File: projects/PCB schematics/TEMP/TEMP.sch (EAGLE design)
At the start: 0 parts

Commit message: POWER - Initial drafts.
Adding in initial place holders for DCDC, 5V, and 12V. Completed most of TEMP.
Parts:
- added IC1, IC10, IC2, IC3, IC4, IC5, IC6, IC7, IC8, IC9: 4051D, 40xx:4051D
- added J1, J2: SAMTEC-TFM-120-02-X-D-LCJ, SAMTEC-TFM-120-02-X-D-LC:SAMTEC-TFM-120-02-X-D-LCJ
- added R1, R2, R3, R4: (no value), rcl:R-US_R0805
- added X2: 5566-4, con-molex:5566-4
- added X3: 5566-2, con-molex:5566-2
- added X4: 5566-10, con-molex:5566-10
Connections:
- new net CS_A: IC10A.A, IC1A.A, IC2A.A, IC3A.A, IC4A.A, IC5A.A, IC6A.A, IC7A.A, IC8A.A, IC9A.A, R2.2, X2-1.S
- new net CS_B: IC10A.B, IC1A.B, IC2A.B, IC3A.B, IC4A.B, IC5A.B, IC6A.B, IC7A.B, IC8A.B, IC9A.B, R3.2, X2-2.S
- new net CS_C: IC10A.C, IC1A.C, IC2A.C, IC3A.C, IC4A.C, IC5A.C, IC6A.C, IC7A.C, IC8A.C, IC9A.C, R4.2, X2-3.S
- new net GND: R1.1, R2.1, R3.1, R4.1, X3-2.S
- new net INH: IC10A.INH, IC1A.INH, IC2A.INH, IC3A.INH, IC4A.INH, IC5A.INH, IC6A.INH, IC7A.INH, IC8A.INH, IC9A.INH, R1.2
- new net TEMP1: IC1A.X0, J1.1
- new net TEMP10: IC2A.X1, J1.10
- new net TEMP11: IC2A.X2, J1.11
- new net TEMP12: IC2A.X3, J1.12
- new net TEMP13: IC2A.X4, J1.13
- new net TEMP14: IC2A.X5, J1.14
- new net TEMP15: IC2A.X6, J1.15
- new net TEMP16: IC2A.X7, J1.16
- new net TEMP17: IC3A.X0, J1.17
- new net TEMP18: IC3A.X1, J1.18
- new net TEMP19: IC3A.X2, J1.19
- new net TEMP2: IC1A.X1, J1.2
- new net TEMP20: IC3A.X3, J1.20
- new net TEMP21: IC3A.X4, J1.21
- new net TEMP22: IC3A.X5, J1.22
- new net TEMP23: IC3A.X6, J1.23
- new net TEMP24: IC3A.X7, J1.24
- new net TEMP25: IC5A.X0, J1.25
- new net TEMP26: IC5A.X1, J1.26
- new net TEMP27: IC5A.X2, J1.27
- new net TEMP28: IC5A.X3, J1.28
- new net TEMP29: IC5A.X4, J1.29
- new net TEMP3: IC1A.X2, J1.3
- new net TEMP30: IC5A.X5, J1.30
- new net TEMP31: IC5A.X6, J1.31
- new net TEMP32: IC5A.X7, J1.32
- new net TEMP33: IC6A.X0, J1.33
- new net TEMP34: IC6A.X1, J1.34
- new net TEMP35: IC6A.X2, J1.35
- new net TEMP36: IC6A.X3, J1.36
- new net TEMP37: IC6A.X4, J1.37
- new net TEMP38: IC6A.X5, J1.38
- new net TEMP39: IC6A.X6, J1.39
- new net TEMP4: IC1A.X3, J1.4
- new net TEMP40: IC6A.X7, J1.40
- new net TEMP41: IC7A.X0, J2.1
- new net TEMP42: IC7A.X1, J2.2
- new net TEMP43: IC7A.X2, J2.3
- new net TEMP44: IC7A.X3, J2.4
- new net TEMP45: IC7A.X4, J2.5
- new net TEMP46: IC7A.X5, J2.6
- new net TEMP47: IC7A.X6, J2.7
- new net TEMP48: IC7A.X7, J2.8
- new net TEMP49: IC4A.X0, J2.9
- new net TEMP5: IC1A.X4, J1.5
- new net TEMP50: IC4A.X1, J2.10
- new net TEMP51: IC4A.X2, J2.11
- new net TEMP52: IC4A.X3, J2.12
- new net TEMP53: IC4A.X4, J2.13
- new net TEMP54: IC4A.X5, J2.14
- new net TEMP55: IC4A.X6, J2.15
- new net TEMP56: IC4A.X7, J2.16
- new net TEMP57: IC9A.X0, J2.17
- new net TEMP58: IC9A.X1, J2.18
- new net TEMP59: IC9A.X2, J2.19
- new net TEMP6: IC1A.X5, J1.6
- new net TEMP60: IC9A.X3, J2.20
- new net TEMP61: IC9A.X4, J2.21
- new net TEMP62: IC9A.X5, J2.22
- new net TEMP63: IC9A.X6, J2.23
- new net TEMP64: IC9A.X7, J2.24
- new net TEMP65: IC8A.X0, J2.25
- new net TEMP66: IC8A.X1, J2.26
- new net TEMP67: IC8A.X2, J2.27
- new net TEMP68: IC8A.X3, J2.28
- new net TEMP69: IC8A.X4, J2.29
- new net TEMP7: IC1A.X6, J1.7
- new net TEMP70: IC8A.X5, J2.30
- new net TEMP71: IC8A.X6, J2.31
- new net TEMP72: IC8A.X7, J2.32
- new net TEMP73: IC10A.X0, J2.33
- new net TEMP74: IC10A.X1, J2.34
- new net TEMP75: IC10A.X2, J2.35
- new net TEMP76: IC10A.X3, J2.36
- new net TEMP77: IC10A.X4, J2.37
- new net TEMP78: IC10A.X5, J2.38
- new net TEMP79: IC10A.X6, J2.39
- new net TEMP8: IC1A.X7, J1.8
- new net TEMP80: IC10A.X7, J2.40
- new net TEMP9: IC2A.X0, J1.9
- new net TEMP_OUT1: IC1A.X, X4-1.S
- new net TEMP_OUT10: IC10A.X, X4-10.S
- new net TEMP_OUT2: IC2A.X, X4-2.S
- new net TEMP_OUT3: IC3A.X, X4-3.S
- new net TEMP_OUT4: IC5A.X, X4-4.S
- new net TEMP_OUT5: IC6A.X, X4-5.S
- new net TEMP_OUT6: IC7A.X, X4-6.S
- new net TEMP_OUT7: IC4A.X, X4-7.S
- new net TEMP_OUT8: IC9A.X, X4-8.S
- new net TEMP_OUT9: IC8A.X, X4-9.S
- new net VCC: X3-1.S

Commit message: TEMP - Initial board placement.
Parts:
- removed IC1, IC10, IC2, IC3, IC4, IC5, IC6, IC7, IC8, IC9: 4051D, 40xx:4051D
- removed J2: SAMTEC-TFM-120-02-X-D-LCJ, SAMTEC-TFM-120-02-X-D-LC:SAMTEC-TFM-120-02-X-D-LCJ
- added MUX1, MUX2, MUX3, MUX4, MUX5: 4051D, 40xx:4051D
- added SH1, SH2, SH3: SHORTT5, shorts:SHORTT5
- added X1: 5566-4, con-molex:5566-4
- R1, R2, R3, R4: value (none) -> 50k
- X4: value 5566-10 -> 5566-6; device con-molex:5566-10 -> con-molex:5566-6
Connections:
- removed net CS_A: IC10A.A, IC1A.A, IC2A.A, IC3A.A, IC4A.A, IC5A.A, IC6A.A, IC7A.A, IC8A.A, IC9A.A, R2.2, X2-1.S
- removed net CS_B: IC10A.B, IC1A.B, IC2A.B, IC3A.B, IC4A.B, IC5A.B, IC6A.B, IC7A.B, IC8A.B, IC9A.B, R3.2, X2-2.S
- removed net CS_C: IC10A.C, IC1A.C, IC2A.C, IC3A.C, IC4A.C, IC5A.C, IC6A.C, IC7A.C, IC8A.C, IC9A.C, R4.2, X2-3.S
- removed net TEMP41: IC7A.X0, J2.1
- removed net TEMP42: IC7A.X1, J2.2
- removed net TEMP43: IC7A.X2, J2.3
- removed net TEMP44: IC7A.X3, J2.4
- removed net TEMP45: IC7A.X4, J2.5
- removed net TEMP46: IC7A.X5, J2.6
- removed net TEMP47: IC7A.X6, J2.7
- removed net TEMP48: IC7A.X7, J2.8
- removed net TEMP49: IC4A.X0, J2.9
- removed net TEMP50: IC4A.X1, J2.10
- removed net TEMP51: IC4A.X2, J2.11
- removed net TEMP52: IC4A.X3, J2.12
- removed net TEMP53: IC4A.X4, J2.13
- removed net TEMP54: IC4A.X5, J2.14
- removed net TEMP55: IC4A.X6, J2.15
- removed net TEMP56: IC4A.X7, J2.16
- removed net TEMP57: IC9A.X0, J2.17
- removed net TEMP58: IC9A.X1, J2.18
- removed net TEMP59: IC9A.X2, J2.19
- removed net TEMP60: IC9A.X3, J2.20
- removed net TEMP61: IC9A.X4, J2.21
- removed net TEMP62: IC9A.X5, J2.22
- removed net TEMP63: IC9A.X6, J2.23
- removed net TEMP64: IC9A.X7, J2.24
- removed net TEMP65: IC8A.X0, J2.25
- removed net TEMP66: IC8A.X1, J2.26
- removed net TEMP67: IC8A.X2, J2.27
- removed net TEMP68: IC8A.X3, J2.28
- removed net TEMP69: IC8A.X4, J2.29
- removed net TEMP70: IC8A.X5, J2.30
- removed net TEMP71: IC8A.X6, J2.31
- removed net TEMP72: IC8A.X7, J2.32
- removed net TEMP73: IC10A.X0, J2.33
- removed net TEMP74: IC10A.X1, J2.34
- removed net TEMP75: IC10A.X2, J2.35
- removed net TEMP76: IC10A.X3, J2.36
- removed net TEMP77: IC10A.X4, J2.37
- removed net TEMP78: IC10A.X5, J2.38
- removed net TEMP79: IC10A.X6, J2.39
- removed net TEMP80: IC10A.X7, J2.40
- removed net TEMP_OUT10: IC10A.X, X4-10.S
- removed net TEMP_OUT6: IC7A.X, X4-6.S
- removed net TEMP_OUT7: IC4A.X, X4-7.S
- removed net TEMP_OUT8: IC9A.X, X4-8.S
- removed net TEMP_OUT9: IC8A.X, X4-9.S
- new net CS_A_IN: MUX1A.A, MUX2A.A, MUX3A.A, MUX4A.A, MUX5A.A, R2.2, SH1.P$1, X2-1.S
- new net CS_A_OUT: SH1.P$2, X1-1.S
- new net CS_B_IN: MUX1A.B, MUX2A.B, MUX3A.B, MUX4A.B, MUX5A.B, R3.2, SH2.P$1, X2-2.S
- new net CS_B_OUT: SH2.P$2, X1-2.S
- new net CS_C_IN: MUX1A.C, MUX2A.C, MUX3A.C, MUX4A.C, MUX5A.C, R4.2, SH3.P$1, X2-3.S
- new net CS_C_OUT: SH3.P$2, X1-3.S
- net GND: now also MUX1P.GND, MUX1P.VEE, MUX2P.GND, MUX2P.VEE, MUX3P.GND, MUX3P.VEE, MUX4P.GND, MUX4P.VEE, MUX5P.GND, MUX5P.VEE
- net INH: now also MUX1A.INH, MUX2A.INH, MUX3A.INH, MUX4A.INH, MUX5A.INH; no longer IC10A.INH, IC1A.INH, IC2A.INH, IC3A.INH, IC4A.INH, IC5A.INH, IC6A.INH, IC7A.INH, IC8A.INH, IC9A.INH
- net TEMP1: now also MUX1A.X0; no longer IC1A.X0
- net TEMP10: now also MUX2A.X1; no longer IC2A.X1
- net TEMP11: now also MUX2A.X2; no longer IC2A.X2
- net TEMP12: now also MUX2A.X3; no longer IC2A.X3
- net TEMP13: now also MUX2A.X4; no longer IC2A.X4
- net TEMP14: now also MUX2A.X5; no longer IC2A.X5
- net TEMP15: now also MUX2A.X6; no longer IC2A.X6
- net TEMP16: now also MUX2A.X7; no longer IC2A.X7
- net TEMP17: now also MUX3A.X0; no longer IC3A.X0
- net TEMP18: now also MUX3A.X1; no longer IC3A.X1
- net TEMP19: now also MUX3A.X2; no longer IC3A.X2
- net TEMP2: now also MUX1A.X1; no longer IC1A.X1
- net TEMP20: now also MUX3A.X3; no longer IC3A.X3
- net TEMP21: now also MUX3A.X4; no longer IC3A.X4
- net TEMP22: now also MUX3A.X5; no longer IC3A.X5
- net TEMP23: now also MUX3A.X6; no longer IC3A.X6
- net TEMP24: now also MUX3A.X7; no longer IC3A.X7
- net TEMP25: now also MUX4A.X0; no longer IC5A.X0
- net TEMP26: now also MUX4A.X1; no longer IC5A.X1
- net TEMP27: now also MUX4A.X2; no longer IC5A.X2
- net TEMP28: now also MUX4A.X3; no longer IC5A.X3
- net TEMP29: now also MUX4A.X4; no longer IC5A.X4
- net TEMP3: now also MUX1A.X2; no longer IC1A.X2
- net TEMP30: now also MUX4A.X5; no longer IC5A.X5
- net TEMP31: now also MUX4A.X6; no longer IC5A.X6
- net TEMP32: now also MUX4A.X7; no longer IC5A.X7
- net TEMP33: now also MUX5A.X0; no longer IC6A.X0
- net TEMP34: now also MUX5A.X1; no longer IC6A.X1
- net TEMP35: now also MUX5A.X2; no longer IC6A.X2
- net TEMP36: now also MUX5A.X3; no longer IC6A.X3
- net TEMP37: now also MUX5A.X4; no longer IC6A.X4
- net TEMP38: now also MUX5A.X5; no longer IC6A.X5
- net TEMP39: now also MUX5A.X6; no longer IC6A.X6
- net TEMP4: now also MUX1A.X3; no longer IC1A.X3
- net TEMP40: now also MUX5A.X7; no longer IC6A.X7
- net TEMP5: now also MUX1A.X4; no longer IC1A.X4
- net TEMP6: now also MUX1A.X5; no longer IC1A.X5
- net TEMP7: now also MUX1A.X6; no longer IC1A.X6
- net TEMP8: now also MUX1A.X7; no longer IC1A.X7
- net TEMP9: now also MUX2A.X0; no longer IC2A.X0
- net TEMP_OUT1: now also MUX1A.X; no longer IC1A.X
- net TEMP_OUT2: now also MUX2A.X; no longer IC2A.X
- net TEMP_OUT3: now also MUX3A.X; no longer IC3A.X
- net TEMP_OUT4: now also MUX4A.X; no longer IC5A.X
- net TEMP_OUT5: now also MUX5A.X; no longer IC6A.X
- net VCC: now also MUX1P.VCC, MUX2P.VCC
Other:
- moved on the sheet: J1, R1, R2, R3, R4, X2-1, X2-2, X2-3, X2-4, X3-1, X3-2, X4-1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

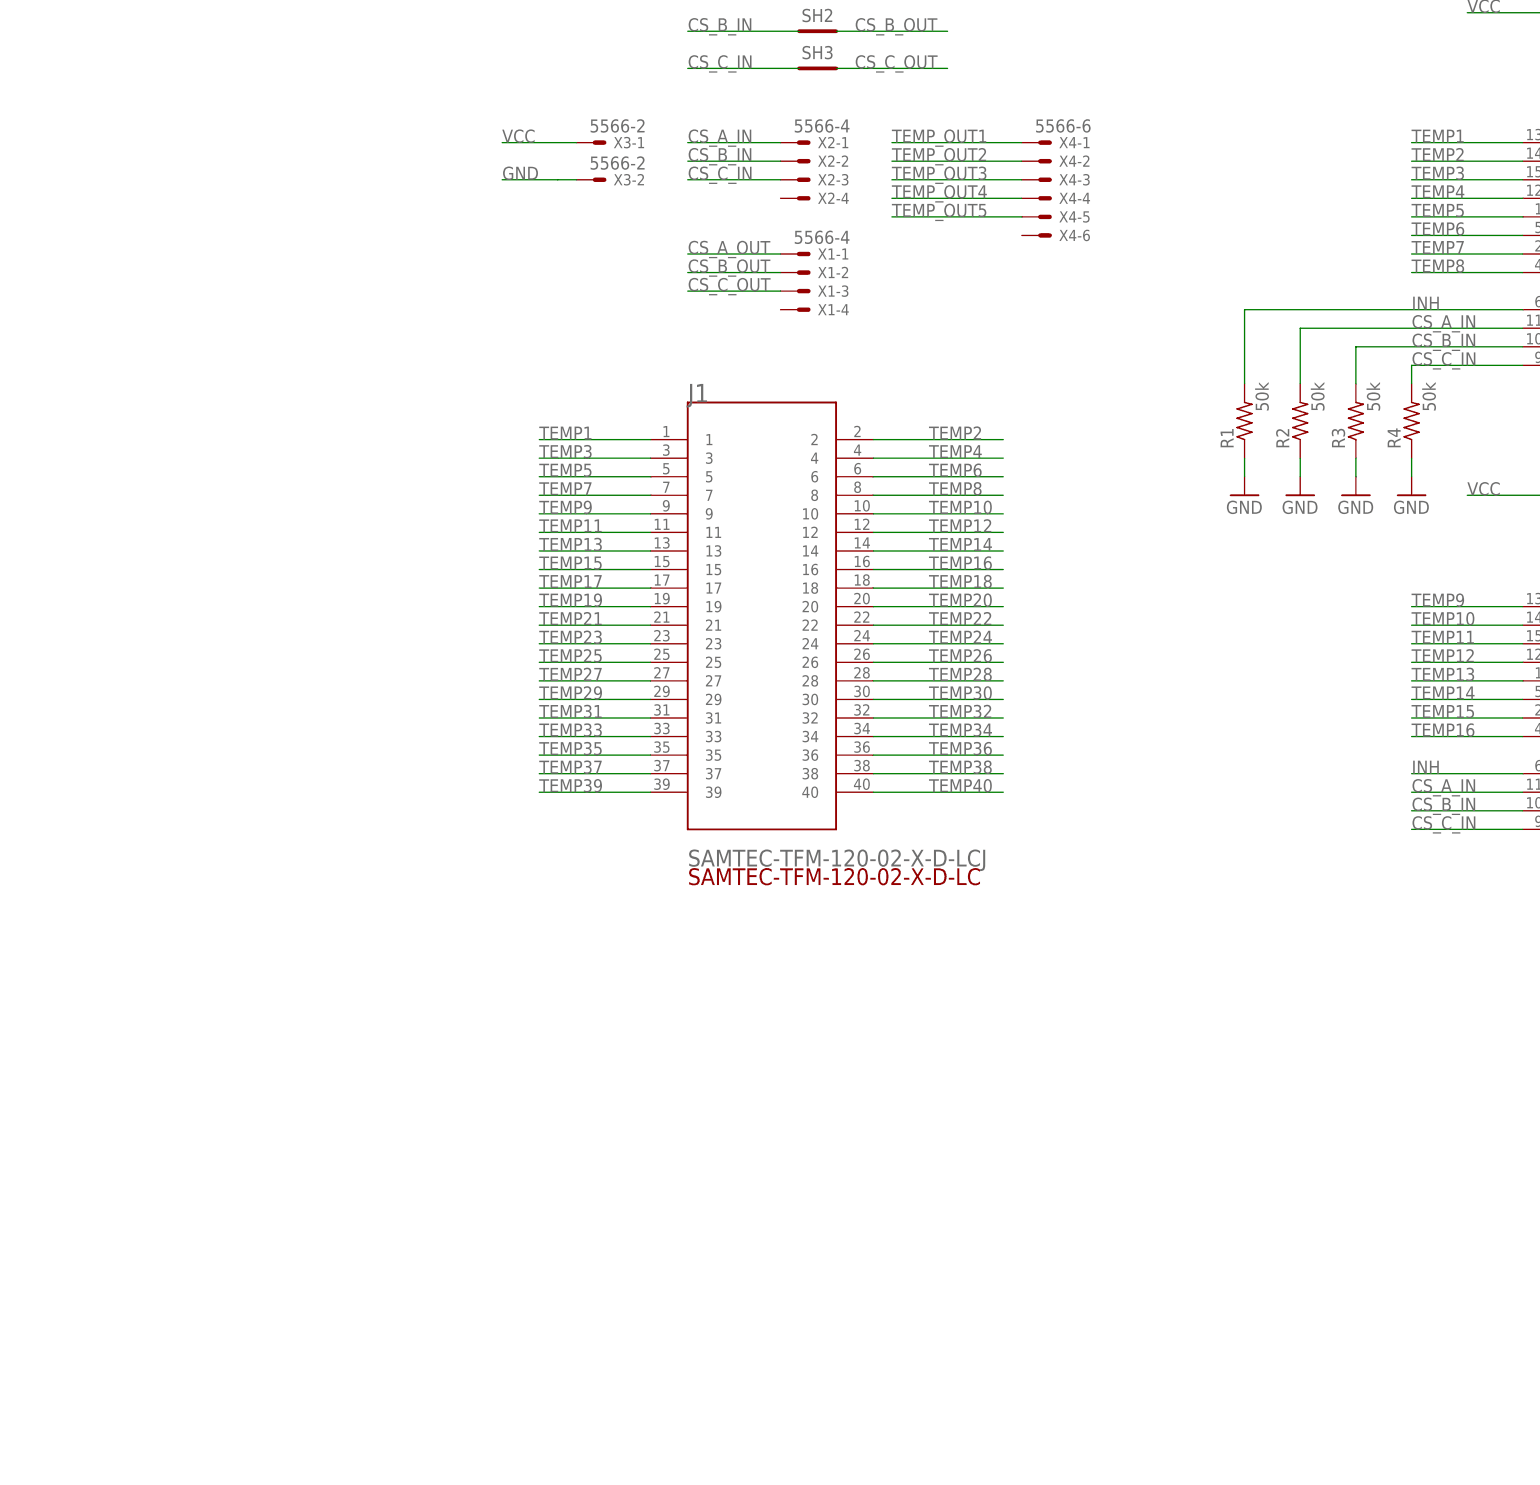
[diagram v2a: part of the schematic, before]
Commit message: TEMP - Energus components added in.
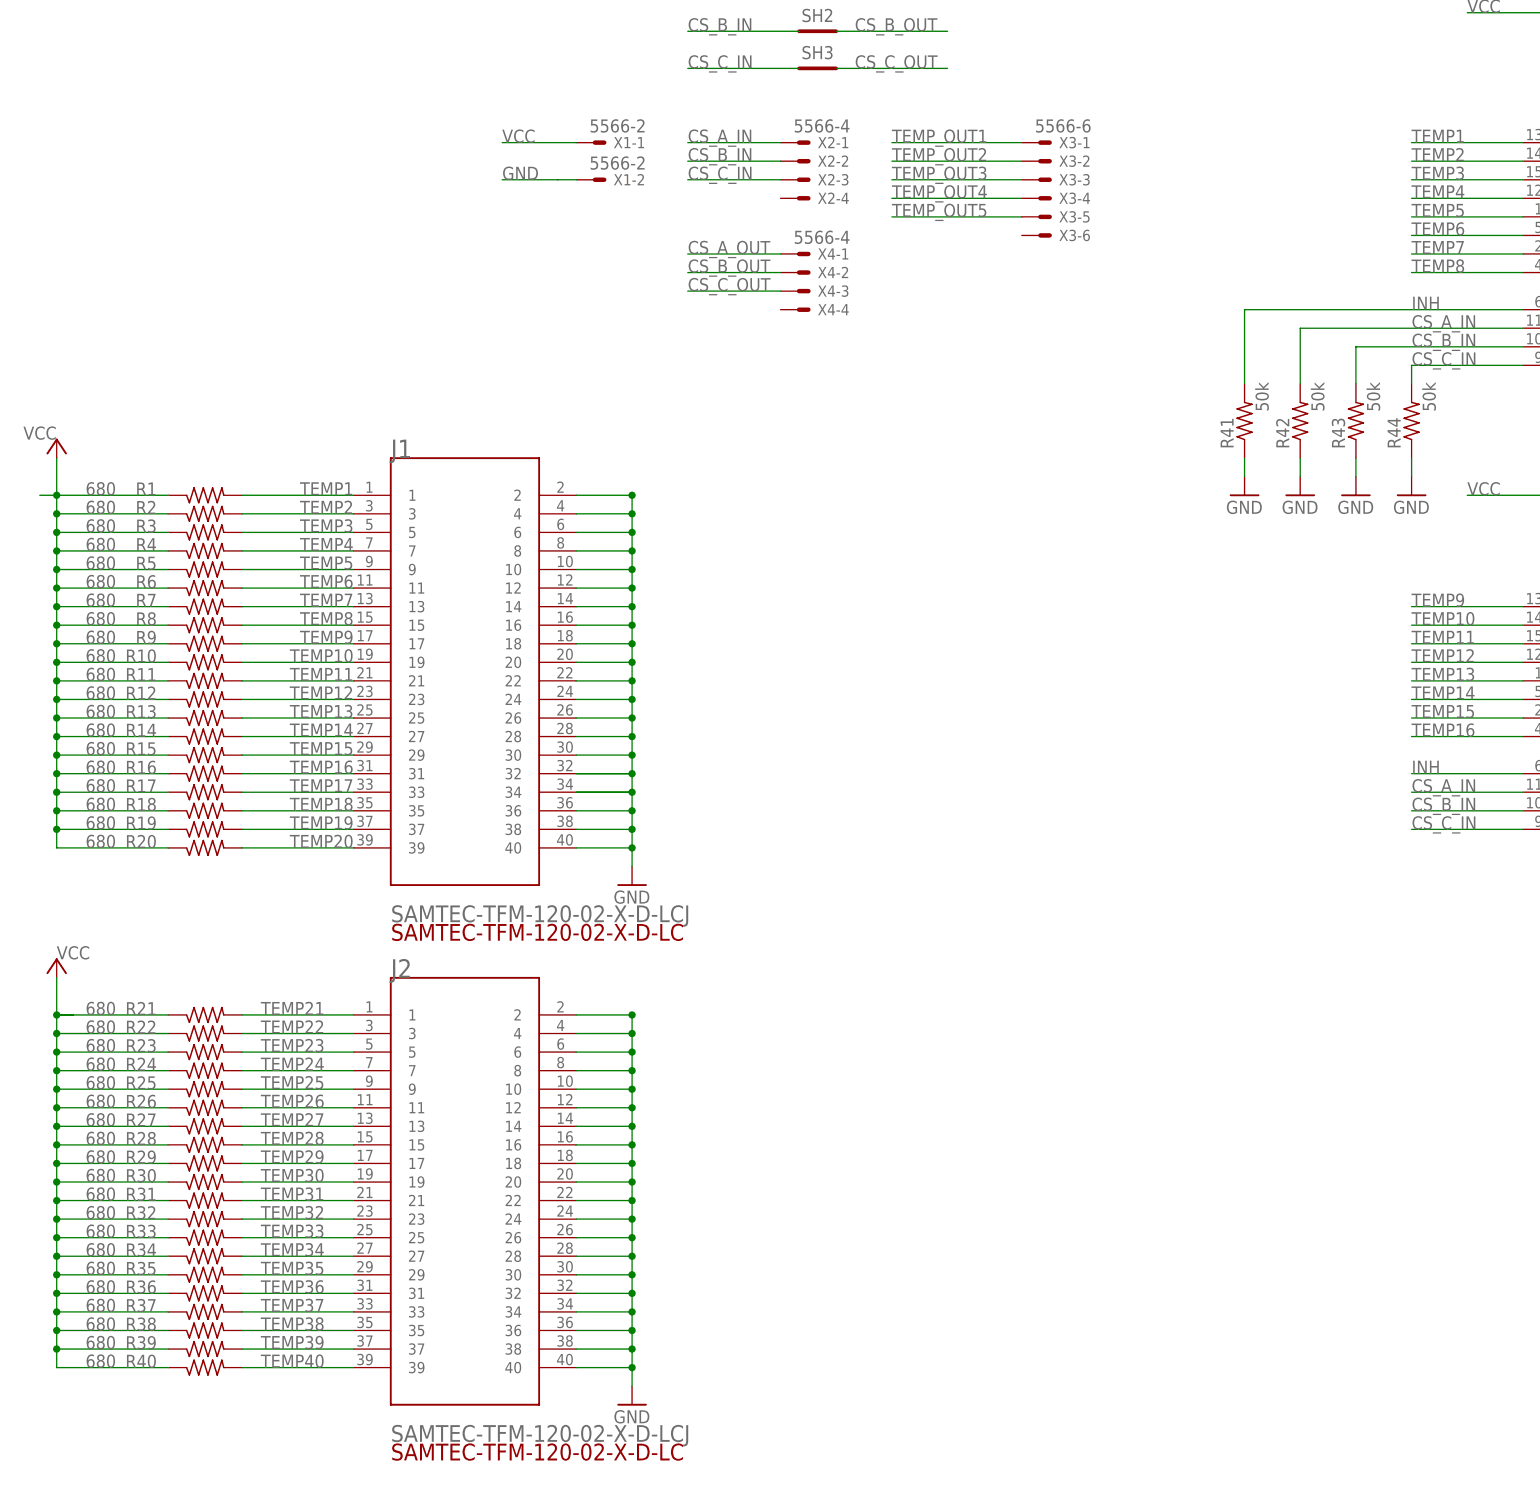
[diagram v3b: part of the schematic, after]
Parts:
- added J2: SAMTEC-TFM-120-02-X-D-LCJ, SAMTEC-TFM-120-02-X-D-LC:SAMTEC-TFM-120-02-X-D-LCJ
- added R10, R11, R12, R13, R14, R15, R16, R17, R18, R19, R20, R21, R22, R23, R24, R25, R26, R27, R28, R29, R30, R31, R32, R33, R34, R35, R36, R37, R38, R39, R40, R5, R6, R7, R8, R9: 680, rcl:R-US_R0805
- added R41, R42, R43, R44: 50k, rcl:R-US_R0805
- R1, R2, R3, R4: value 50k -> 680
- X1: value 5566-4 -> 5566-2; device con-molex:5566-4 -> con-molex:5566-2
- X3: value 5566-2 -> 5566-6; device con-molex:5566-2 -> con-molex:5566-6
- X4: value 5566-6 -> 5566-4; device con-molex:5566-6 -> con-molex:5566-4
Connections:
- net CS_A_IN: now also R42.2; no longer R2.2
- net CS_A_OUT: now also X4-1.S; no longer X1-1.S
- net CS_B_IN: now also R43.2; no longer R3.2
- net CS_B_OUT: now also X4-2.S; no longer X1-2.S
- net CS_C_IN: now also R44.2; no longer R4.2
- net CS_C_OUT: now also X4-3.S; no longer X1-3.S
- net GND: now also J1.10, J1.12, J1.14, J1.16, J1.18, J1.2, J1.20, J1.22, J1.24, J1.26, J1.28, J1.30, J1.32, J1.34, J1.36, J1.38, J1.4, J1.40, J1.6, J1.8, J2.10, J2.12, J2.14, J2.16, J2.18, J2.2, J2.20, J2.22, J2.24, J2.26, J2.28, J2.30, J2.32, J2.34, J2.36, J2.38, J2.4, J2.40, J2.6, J2.8, R41.1, R42.1, R43.1, R44.1, X1-2.S; no longer R1.1, R2.1, R3.1, R4.1, X3-2.S
- net INH: now also R41.2; no longer R1.2
- net TEMP1: now also R1.2
- net TEMP10: now also J1.19, R10.2; no longer J1.10
- net TEMP11: now also J1.21, R11.2; no longer J1.11
- net TEMP12: now also J1.23, R12.2; no longer J1.12
- net TEMP13: now also J1.25, R13.2; no longer J1.13
- net TEMP14: now also J1.27, R14.2; no longer J1.14
- net TEMP15: now also J1.29, R15.2; no longer J1.15
- net TEMP16: now also J1.31, R16.2; no longer J1.16
- net TEMP17: now also J1.33, R17.2; no longer J1.17
- net TEMP18: now also J1.35, R18.2; no longer J1.18
- net TEMP19: now also J1.37, R19.2; no longer J1.19
- net TEMP2: now also J1.3, R2.2; no longer J1.2
- net TEMP20: now also J1.39, R20.2; no longer J1.20
- net TEMP21: now also J2.1, R21.2; no longer J1.21
- net TEMP22: now also J2.3, R22.2; no longer J1.22
- net TEMP23: now also J2.5, R23.2; no longer J1.23
- net TEMP24: now also J2.7, R24.2; no longer J1.24
- net TEMP25: now also J2.9, R25.2; no longer J1.25
- net TEMP26: now also J2.11, R26.2; no longer J1.26
- net TEMP27: now also J2.13, R27.2; no longer J1.27
- net TEMP28: now also J2.15, R28.2; no longer J1.28
- net TEMP29: now also J2.17, R29.2; no longer J1.29
- net TEMP3: now also J1.5, R3.2; no longer J1.3
- net TEMP30: now also J2.19, R30.2; no longer J1.30
- net TEMP31: now also J2.21, R31.2; no longer J1.31
- net TEMP32: now also J2.23, R32.2; no longer J1.32
- net TEMP33: now also J2.25, R33.2; no longer J1.33
- net TEMP34: now also J2.27, R34.2; no longer J1.34
- net TEMP35: now also J2.29, R35.2; no longer J1.35
- net TEMP36: now also J2.31, R36.2; no longer J1.36
- net TEMP37: now also J2.33, R37.2; no longer J1.37
- net TEMP38: now also J2.35, R38.2; no longer J1.38
- net TEMP39: now also J2.37, R39.2; no longer J1.39
- net TEMP4: now also J1.7, R4.2; no longer J1.4
- net TEMP40: now also J2.39, R40.2; no longer J1.40
- net TEMP5: now also J1.9, R5.2; no longer J1.5
- net TEMP6: now also J1.11, R6.2; no longer J1.6
- net TEMP7: now also J1.13, R7.2; no longer J1.7
- net TEMP8: now also J1.15, R8.2; no longer J1.8
- net TEMP9: now also J1.17, R9.2; no longer J1.9
- net TEMP_OUT1: now also X3-1.S; no longer X4-1.S
- net TEMP_OUT2: now also X3-2.S; no longer X4-2.S
- net TEMP_OUT3: now also X3-3.S; no longer X4-3.S
- net TEMP_OUT4: now also X3-4.S; no longer X4-4.S
- net TEMP_OUT5: now also X3-5.S; no longer X4-5.S
- net VCC: now also R1.1, R10.1, R11.1, R12.1, R13.1, R14.1, R15.1, R16.1, R17.1, R18.1, R19.1, R2.1, R20.1, R21.1, R22.1, R23.1, R24.1, R25.1, R26.1, R27.1, R28.1, R29.1, R3.1, R30.1, R31.1, R32.1, R33.1, R34.1, R35.1, R36.1, R37.1, R38.1, R39.1, R4.1, R40.1, R5.1, R6.1, R7.1, R8.1, R9.1, X1-1.S; no longer X3-1.S
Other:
- moved on the sheet: J1, R1, R2, R3, R4, X1-1, X1-2, X3-1, X3-2, X4-1, X4-2, X4-3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
